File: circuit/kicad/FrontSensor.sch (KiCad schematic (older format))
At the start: 18 parts, among them J1 FFC6, Q1 TEMT7100X01, Q2 TEMT7100X01, Q3 TEMT7100X01, Q4 TEMT7100X01

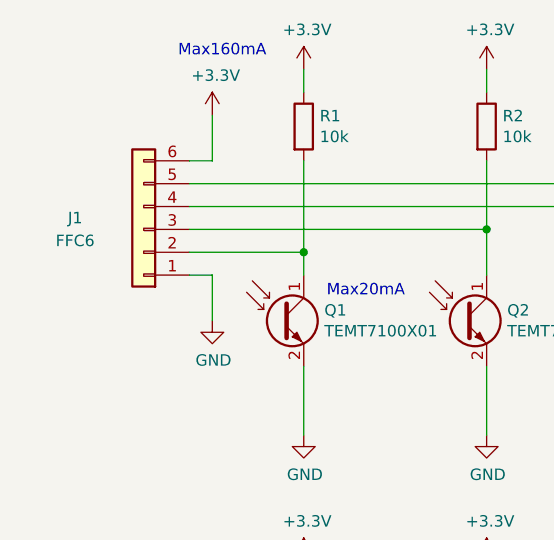
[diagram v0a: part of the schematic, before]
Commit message: あとはシルクを見やすい位置にもっていくだけ。
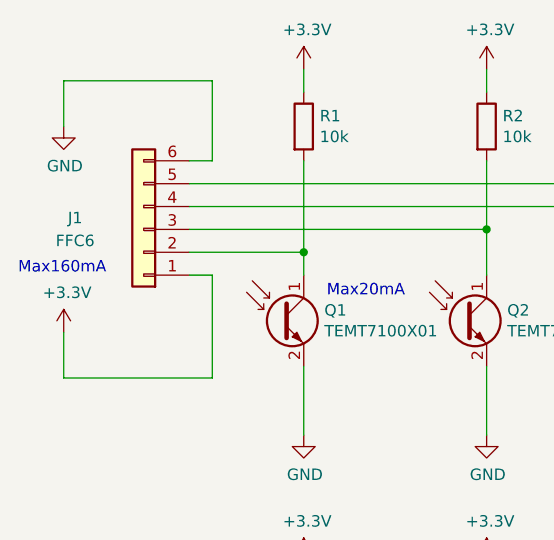
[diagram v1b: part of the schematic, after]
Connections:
- net +3V3: now also J1.1 (Pin_1); no longer J1.6 (Pin_6)
- net GND: now also J1.6 (Pin_6); no longer J1.1 (Pin_1)
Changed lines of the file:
@@
 $Descr A4 11693 8268
 encoding utf-8
-Sheet 2 5
+Sheet 1 1
 Title ""
 Date ""
@@
 L power:GND #PWR08
 U 1 1 61F65719
-P 4150 3200
-F 0 "#PWR08" H 4150 2950 50  0001 C CNN
-F 1 "GND" H 4155 3027 50  0000 C CNN
-F 2 "" H 4150 3200 50  0001 C CNN
-F 3 "" H 4150 3200 50  0001 C CNN
-	1    4150 3200
-	1    0    0    -1
-$EndComp
-Wire Wire Line
-	4150 3000 4050 3000
+P 3500 2350
+F 0 "#PWR08" H 3500 2100 50  0001 C CNN
+F 1 "GND" H 3505 2177 50  0000 C CNN
+F 2 "" H 3500 2350 50  0001 C CNN
+F 3 "" H 3500 2350 50  0001 C CNN
+	1    3500 2350
+	1    0    0    -1
+$EndComp
 $Comp
 L power:+3.3V #PWR05
 U 1 1 61F65720
-P 4150 2300
-F 0 "#PWR05" H 4150 2150 50  0001 C CNN
-F 1 "+3.3V" H 4165 2473 50  0000 C CNN
-F 2 "" H 4150 2300 50  0001 C CNN
-F 3 "" H 4150 2300 50  0001 C CNN
-	1    4150 2300
-	1    0    0    -1
-$EndComp
-Wire Wire Line
-	4150 2500 4050 2500
+P 3500 3250
+F 0 "#PWR05" H 3500 3100 50  0001 C CNN
+F 1 "+3.3V" H 3515 3423 50  0000 C CNN
+F 2 "" H 3500 3250 50  0001 C CNN
+F 3 "" H 3500 3250 50  0001 C CNN
+	1    3500 3250
+	1    0    0    -1
+$EndComp
 $Comp
 L Device:C C1
@@
 Text Notes 4700 5150 0    50   ~ 0
 20mA
-Text Notes 4000 2050 0    50   ~ 0
+Text Notes 3300 3000 0    50   ~ 0
 Max160mA
 Wire Wire Line
-	4150 2300 4150 2500
-Wire Wire Line
-	4150 3000 4150 3200
+	3500 3250 3500 3450
+Wire Wire Line
+	3500 2150 3500 2350
 Wire Wire Line
 	4050 2600 6950 2600
@@
 Connection ~ 6150 2700
 $Comp
-L power:PWR_FLAG #FLG?
+L power:PWR_FLAG #FLG0101
 U 1 1 61F7BEDF
 P 5250 7300
-F 0 "#FLG?" H 5250 7375 50  0001 C CNN
+F 0 "#FLG0101" H 5250 7375 50  0001 C CNN
 F 1 "PWR_FLAG" H 5250 7473 50  0000 C CNN
 F 2 "" H 5250 7300 50  0001 C CNN
@@
 	5250 7300 5250 6800
 $Comp
-L power:PWR_FLAG #FLG?
+L power:PWR_FLAG #FLG0102
 U 1 1 61F7BEE6
 P 5750 7300
-F 0 "#FLG?" H 5750 7375 50  0001 C CNN
+F 0 "#FLG0102" H 5750 7375 50  0001 C CNN
 F 1 "PWR_FLAG" H 5750 7473 50  0000 C CNN
 F 2 "" H 5750 7300 50  0001 C CNN
@@
 	5750 7300 5750 6800
 $Comp
-L power:PWR_FLAG #FLG?
+L power:PWR_FLAG #FLG0103
 U 1 1 61F7BEED
 P 6250 6800
-F 0 "#FLG?" H 6250 6875 50  0001 C CNN
+F 0 "#FLG0103" H 6250 6875 50  0001 C CNN
 F 1 "PWR_FLAG" H 6250 6973 50  0000 C CNN
 F 2 "" H 6250 6800 50  0001 C CNN
@@
 	6250 6800 6250 7300
 $Comp
-L power:+5V #PWR?
+L power:+5V #PWR0101
 U 1 1 61F7BEF4
 P 5250 6800
-F 0 "#PWR?" H 5250 6650 50  0001 C CNN
+F 0 "#PWR0101" H 5250 6650 50  0001 C CNN
 F 1 "+5V" H 5265 6973 50  0000 C CNN
 F 2 "" H 5250 6800 50  0001 C CNN
@@
 $EndComp
 $Comp
-L power:+3.3V #PWR?
+L power:+3.3V #PWR0102
 U 1 1 61F7BEFA
 P 5750 6800
-F 0 "#PWR?" H 5750 6650 50  0001 C CNN
+F 0 "#PWR0102" H 5750 6650 50  0001 C CNN
 F 1 "+3.3V" H 5765 6973 50  0000 C CNN
 F 2 "" H 5750 6800 50  0001 C CNN
@@
 $EndComp
 $Comp
-L power:GND #PWR?
+L power:GND #PWR0103
 U 1 1 61F7BF00
 P 6250 7300
-F 0 "#PWR?" H 6250 7050 50  0001 C CNN
+F 0 "#PWR0103" H 6250 7050 50  0001 C CNN
 F 1 "GND" H 6255 7127 50  0000 C CNN
 F 2 "" H 6250 7300 50  0001 C CNN
@@
 	1    0    0    -1
 $EndComp
+Wire Wire Line
+	3500 2150 4150 2150
+Wire Wire Line
+	4150 2150 4150 2500
+Wire Wire Line
+	4150 2500 4050 2500
+Wire Wire Line
+	4050 3000 4150 3000
+Wire Wire Line
+	4150 3000 4150 3450
+Wire Wire Line
+	4150 3450 3500 3450
 $EndSCHEMATC
